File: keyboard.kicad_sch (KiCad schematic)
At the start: 52 parts, among them J1 TRRS, SW00 Key, SW01 Key, SW02 Key, SW03 Key, SW04 Key, SW05 Key, SW10 Key, SW11 Key, SW12 Key, SW13 Key, SW14 Key, SW15 Key, SW16 Key, SW17 Key, SW18 Key, SW20 Key, SW21 Key, SW22 Key, SW23 Key, SW24 Key, SW25 Key, SW26 Key, SW27 Key, SW28 Key, SW30 Key, SW31 Key, SW32 Key, SW33 Key, SW34 Key, SW35 Key, SW36 Key, SW37 Key, SW38 Key, SW40 Key, SW41 Key, SW42 Key, SW43 Key, SW44 Key, SW45 Key, SW46 Key, SW47 Key, SW48 Key, U1 ProMicro

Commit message: rename files
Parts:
- H1: footprint myles-keyboard:RightPlate -> keyboard:RightPlate; symbol myles-keyboard:RightPate -> keyboard:RightPate
- J1: footprint myles-keyboard:PJ-320A -> keyboard:PJ-320A; symbol myles-keyboard:PJ-320A -> keyboard:PJ-320A
- JP1, JP2: footprint myles-keyboard:Jumper -> keyboard:Jumper; symbol myles-keyboard:Jumper -> keyboard:Jumper
- JP3, JP4: footprint myles-keyboard:JumperSplit -> keyboard:JumperSplit; symbol myles-keyboard:JumperSplit -> keyboard:JumperSplit
- R1, R2: footprint myles-keyboard:SDR18 -> keyboard:SDR18
- SW00, SW04, SW05, SW10, SW14, SW20, SW30: footprint myles-keyboard:KeyLeft -> keyboard:KeyLeft; symbol myles-keyboard:Key -> keyboard:Key
- SW01, SW02, SW11, SW12, SW13, SW15, SW16, SW17, SW21, SW22, SW23, SW24, SW25, SW26, SW27, SW31, SW32, SW33, SW34, SW35, SW36, SW37, SW40, SW41, SW42, SW43, SW44, SW46, SW47: footprint myles-keyboard:Key -> keyboard:Key; symbol myles-keyboard:Key -> keyboard:Key
- SW03, SW18, SW28, SW38, SW45, SW48: footprint myles-keyboard:KeyRight -> keyboard:KeyRight; symbol myles-keyboard:Key -> keyboard:Key
- SW_RST1: footprint myles-keyboard:PTS636 -> keyboard:PTS636; symbol myles-keyboard:SW_Push -> keyboard:SW_Push
- U1: footprint myles-keyboard:ProMicro -> keyboard:ProMicro; symbol myles-keyboard:ProMicro -> keyboard:ProMicro

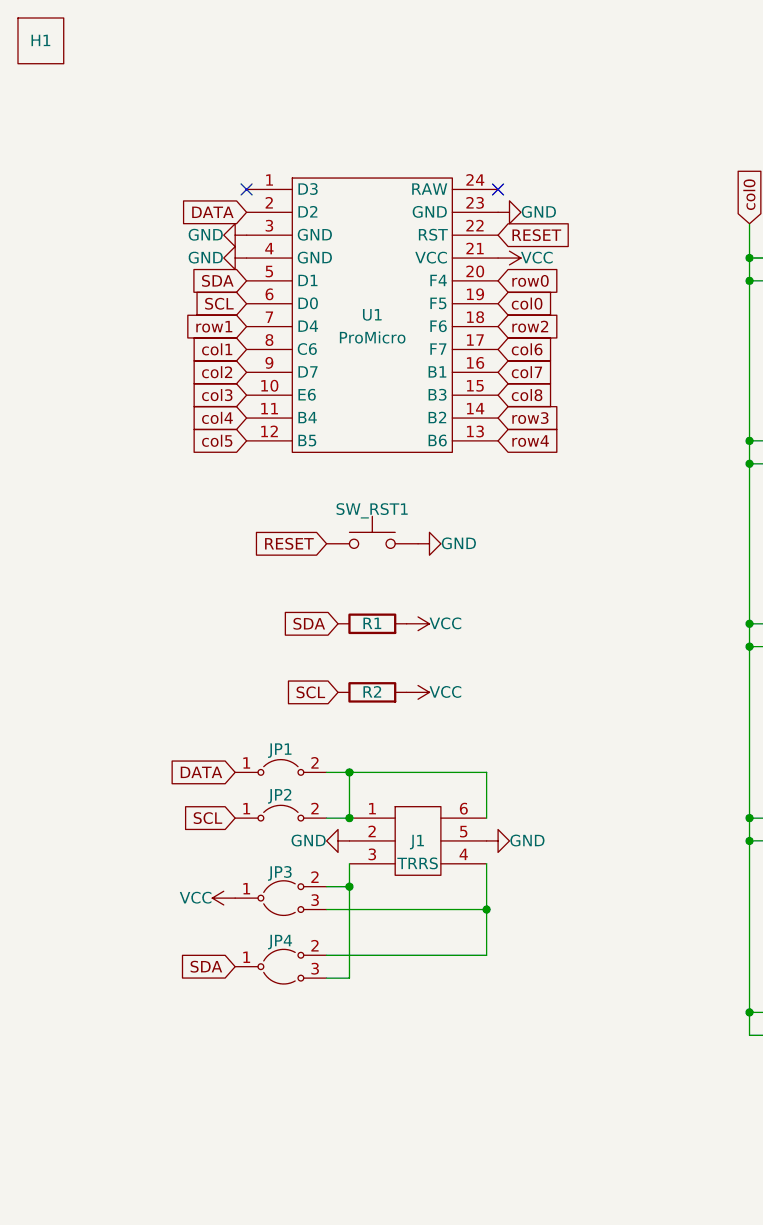
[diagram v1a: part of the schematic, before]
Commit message: add symbol and footprint for new thin reset button
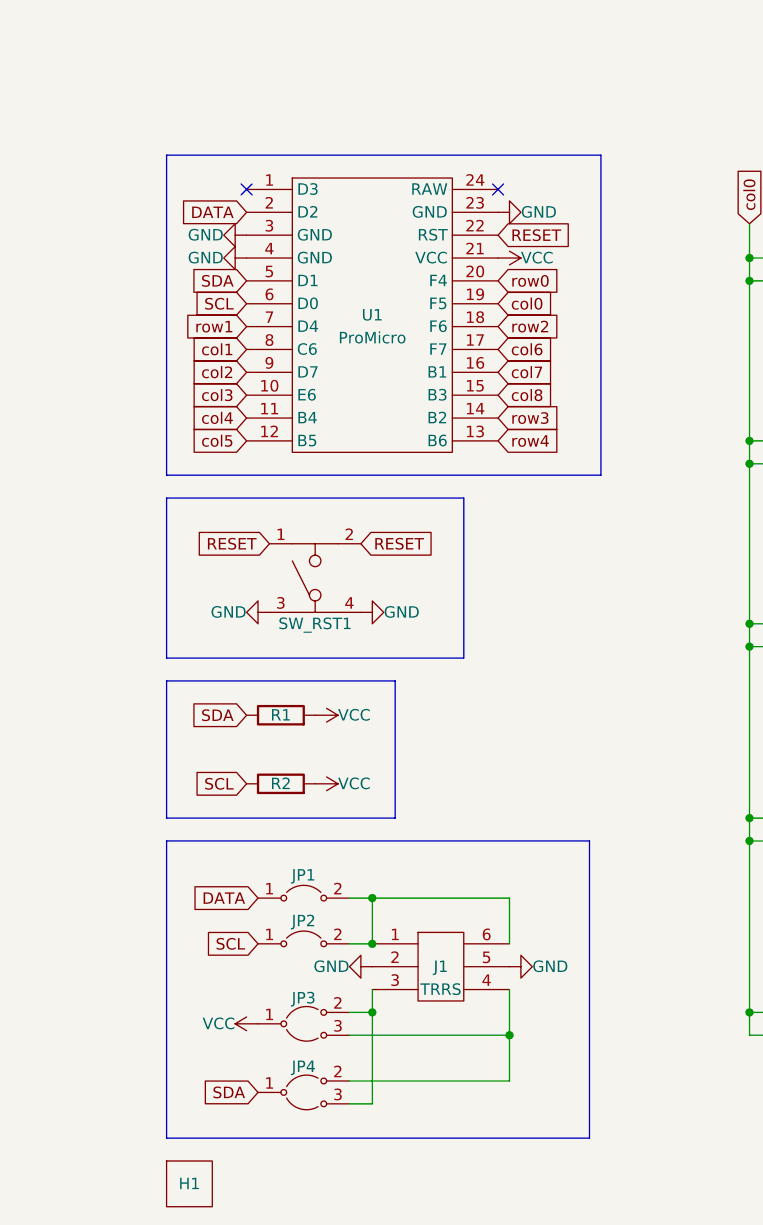
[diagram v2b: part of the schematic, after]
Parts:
- removed SW_RST1: SW_Push, keyboard:PTS636, symbol keyboard:SW_Push
- added SW_RST1: PTS525, keyboard:PTS525, symbol keyboard:PTS525
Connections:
- net GND: now also SW_RST1.3, SW_RST1.4
- net RESET: now also SW_RST1.1, SW_RST1.2
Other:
- moved on the sheet: H1, J1, JP1, JP2, JP3, JP4, R1, R2

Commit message: remove two thumb keys
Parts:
- removed SW04, SW05: Key, keyboard:KeyLeft, symbol keyboard:Key
- SW20, SW30: footprint keyboard:KeyLeft -> keyboard:Key
- SW40, SW41: footprint keyboard:Key -> keyboard:KeyLeft
- SW43: footprint keyboard:Key -> keyboard:KeyRight
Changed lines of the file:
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@@
   (junction (at 219.71 81.28) (diameter 0) (color 0 0 0 0)
   )
-  (junction (at 184.15 43.18) (diameter 0) (color 0 0 0 0)
-  )
   (junction (at 95.25 124.46) (diameter 0) (color 0 0 0 0)
   )
@@
   (junction (at 166.37 60.96) (diameter 0) (color 0 0 0 0)
   )
-  (junction (at 166.37 40.64) (diameter 0) (color 0 0 0 0)
-  )
   (junction (at 148.59 60.96) (diameter 0) (color 0 0 0 0)
   )
@@
   (junction (at 184.15 105.41) (diameter 0) (color 0 0 0 0)
   )
-  (junction (at 184.15 40.64) (diameter 0) (color 0 0 0 0)
-  )
   (junction (at 95.25 105.41) (diameter 0) (color 0 0 0 0)
   )
@@
   (junction (at 144.78 43.18) (diameter 0) (color 0 0 0 0)
   )
-  (junction (at 166.37 43.18) (diameter 0) (color 0 0 0 0)
-  )
   (junction (at 201.93 81.28) (diameter 0) (color 0 0 0 0)
   )
   (junction (at 198.12 83.82) (diameter 0) (color 0 0 0 0)
   )
-  (junction (at 198.12 43.18) (diameter 0) (color 0 0 0 0)
-  )
   (junction (at 95.25 40.64) (diameter 0) (color 0 0 0 0)
   )
   (junction (at 127 63.5) (diameter 0) (color 0 0 0 0)
   )
-  (junction (at 198.12 53.34) (diameter 0) (color 0 0 0 0)
-  )
   (junction (at 162.56 53.34) (diameter 0) (color 0 0 0 0)
   )
@@
   (junction (at 219.71 124.46) (diameter 0) (color 0 0 0 0)
   )
-  (junction (at 180.34 43.18) (diameter 0) (color 0 0 0 0)
-  )
   (junction (at 109.22 43.18) (diameter 0) (color 0 0 0 0)
   )
@@
   (junction (at 180.34 93.98) (diameter 0) (color 0 0 0 0)
   )
-  (junction (at 180.34 53.34) (diameter 0) (color 0 0 0 0)
-  )
   (junction (at 237.49 83.82) (diameter 0) (color 0 0 0 0)
   )
@@
   (no_connect (at 67.31 33.02))
   (no_connect (at 39.37 33.02))
-  (wire (pts (xy 162.56 53.34) (xy 180.34 53.34))
+  (wire (pts (xy 162.56 53.34) (xy 251.46 53.34))
     (stroke (width 0) (type default))
   )
@@
     (stroke (width 0) (type default))
   )
-  (wire (pts (xy 180.34 40.64) (xy 180.34 43.18))
-    (stroke (width 0) (type default))
-  )
   (wire (pts (xy 232.41 102.87) (xy 233.68 102.87))
     (stroke (width 0) (type default))
@@
     (stroke (width 0) (type default))
   )
-  (wire (pts (xy 166.37 36.83) (xy 166.37 40.64))
+  (wire (pts (xy 166.37 36.83) (xy 166.37 60.96))
     (stroke (width 0) (type default))
   )
@@
     (stroke (width 0) (type default))
   )
-  (wire (pts (xy 198.12 53.34) (xy 251.46 53.34))
-    (stroke (width 0) (type default))
-  )
   (wire (pts (xy 127 72.39) (xy 127 73.66))
     (stroke (width 0) (type default))
@@
     (stroke (width 0) (type default))
   )
-  (wire (pts (xy 184.15 40.64) (xy 184.15 43.18))
-    (stroke (width 0) (type default))
-  )
   (wire (pts (xy 251.46 93.98) (xy 233.68 93.98))
     (stroke (width 0) (type default))
@@
     (stroke (width 0) (type default))
   )
-  (wire (pts (xy 166.37 40.64) (xy 168.91 40.64))
-    (stroke (width 0) (type default))
-  )
   (wire (pts (xy 180.34 124.46) (xy 180.34 127))
     (stroke (width 0) (type default))
@@
     (stroke (width 0) (type default))
   )
-  (wire (pts (xy 196.85 43.18) (xy 198.12 43.18))
-    (stroke (width 0) (type default))
-  )
   (wire (pts (xy 130.81 105.41) (xy 130.81 124.46))
     (stroke (width 0) (type default))
@@
     (stroke (width 0) (type default))
   )
-  (wire (pts (xy 184.15 40.64) (xy 186.69 40.64))
-    (stroke (width 0) (type default))
-  )
   (wire (pts (xy 215.9 127) (xy 215.9 128.27))
     (stroke (width 0) (type default))
@@
     (stroke (width 0) (type default))
   )
-  (wire (pts (xy 179.07 40.64) (xy 180.34 40.64))
-    (stroke (width 0) (type default))
-  )
   (wire (pts (xy 50.8 134.62) (xy 53.34 134.62))
     (stroke (width 0) (type default))
@@
     (stroke (width 0) (type default))
   )
-  (wire (pts (xy 166.37 43.18) (xy 166.37 60.96))
-    (stroke (width 0) (type default))
-  )
   (wire (pts (xy 127 81.28) (xy 127 83.82))
     (stroke (width 0) (type default))
@@
     (stroke (width 0) (type default))
   )
-  (wire (pts (xy 180.34 43.18) (xy 179.07 43.18))
-    (stroke (width 0) (type default))
-  )
   (wire (pts (xy 201.93 124.46) (xy 204.47 124.46))
     (stroke (width 0) (type default))
@@
     (stroke (width 0) (type default))
   )
-  (wire (pts (xy 198.12 43.18) (xy 198.12 40.64))
-    (stroke (width 0) (type default))
-  )
   (wire (pts (xy 232.41 105.41) (xy 233.68 105.41))
     (stroke (width 0) (type default))
@@
     (stroke (width 0) (type default))
   )
-  (wire (pts (xy 180.34 44.45) (xy 180.34 43.18))
-    (stroke (width 0) (type default))
-  )
   (wire (pts (xy 127 60.96) (xy 127 63.5))
     (stroke (width 0) (type default))
@@
     (stroke (width 0) (type default))
   )
-  (wire (pts (xy 198.12 52.07) (xy 198.12 53.34))
-    (stroke (width 0) (type default))
-  )
   (wire (pts (xy 161.29 124.46) (xy 162.56 124.46))
     (stroke (width 0) (type default))
@@
     (stroke (width 0) (type default))
   )
-  (wire (pts (xy 180.34 52.07) (xy 180.34 53.34))
-    (stroke (width 0) (type default))
-  )
   (wire (pts (xy 214.63 60.96) (xy 215.9 60.96))
     (stroke (width 0) (type default))
@@
     (stroke (width 0) (type default))
   )
-  (wire (pts (xy 198.12 40.64) (xy 196.85 40.64))
-    (stroke (width 0) (type default))
-  )
   (wire (pts (xy 95.25 81.28) (xy 97.79 81.28))
     (stroke (width 0) (type default))
   )
-  (wire (pts (xy 184.15 36.83) (xy 184.15 40.64))
-    (stroke (width 0) (type default))
-  )
   (wire (pts (xy 53.34 111.76) (xy 50.8 111.76))
     (stroke (width 0) (type default))
@@
     (stroke (width 0) (type default))
   )
-  (wire (pts (xy 198.12 44.45) (xy 198.12 43.18))
-    (stroke (width 0) (type default))
-  )
   (wire (pts (xy 125.73 40.64) (xy 127 40.64))
     (stroke (width 0) (type default))
@@
     (stroke (width 0) (type default))
   )
-  (wire (pts (xy 184.15 43.18) (xy 184.15 60.96))
+  (wire (pts (xy 184.15 36.83) (xy 184.15 60.96))
     (stroke (width 0) (type default))
   )
@@
     (stroke (width 0) (type default))
   )
-  (wire (pts (xy 184.15 43.18) (xy 186.69 43.18))
-    (stroke (width 0) (type default))
-  )
   (wire (pts (xy 107.95 105.41) (xy 109.22 105.41))
     (stroke (width 0) (type default))
@@
     (stroke (width 0) (type default))
   )
-  (wire (pts (xy 180.34 53.34) (xy 198.12 53.34))
-    (stroke (width 0) (type default))
-  )
   (wire (pts (xy 107.95 127) (xy 109.22 127))
     (stroke (width 0) (type default))
@@
     (stroke (width 0) (type default))
   )
-  (wire (pts (xy 166.37 40.64) (xy 166.37 43.18))
-    (stroke (width 0) (type default))
-  )
   (wire (pts (xy 95.25 124.46) (xy 95.25 127))
     (stroke (width 0) (type default))
@@
     (stroke (width 0) (type default))
   )
-  (wire (pts (xy 166.37 43.18) (xy 168.91 43.18))
-    (stroke (width 0) (type default))
-  )
   (wire (pts (xy 162.56 63.5) (xy 162.56 64.77))
     (stroke (width 0) (type default))
@@
     )
   )
-  (symbol (lib_id "keyboard:Key") (at 173.99 41.91 0) (unit 1)
-    (in_bom yes) (on_board yes) (dnp no)
-    (property "Reference" "SW04" (at 173.99 36.195 0) (do_not_autoplace)
-      (effects (font (size 1.27 1.27)))
-    )
-    (property "Value" "Key" (at 173.99 47.625 0) (do_not_autoplace)
-      (effects (font (size 1.27 1.27)) hide)
-    )
-    (property "Footprint" "keyboard:KeyLeft" (at 173.99 41.91 0)
-      (effects (font (size 1.27 1.27)) hide)
-    )
-    (property "Datasheet" "" (at 173.99 41.91 0)
-      (effects (font (size 1.27 1.27)) hide)
-    )
-    (pin "1")
-    (pin "2")
-    (pin "3")
-    (pin "4")
-    (pin "5")
-    (pin "6")
-    (instances
-      (project "keyboard"
-        (path "/55a8c568-8b67-4781-bca4-b9ba3160a3cd"
-          (reference "SW04") (unit 1)
-        )
-      )
-    )
-  )
   (symbol (lib_id "keyboard:Key") (at 227.33 62.23 0) (unit 1)
     (in_bom yes) (on_board yes) (dnp no) (fields_autoplaced)
@@
       (effects (font (size 1.27 1.27)) hide)
     )
-    (property "Footprint" "keyboard:KeyLeft" (at 102.87 82.55 0)
+    (property "Footprint" "keyboard:Key" (at 102.87 82.55 0)
       (effects (font (size 1.27 1.27)) hide)
     )
@@
       (effects (font (size 1.27 1.27)) hide)
     )
-    (property "Footprint" "keyboard:Key" (at 156.21 125.73 0)
+    (property "Footprint" "keyboard:KeyRight" (at 156.21 125.73 0)
       (effects (font (size 1.27 1.27)) hide)
     )
@@
       (effects (font (size 1.27 1.27)) hide)
     )
-    (property "Footprint" "keyboard:KeyLeft" (at 102.87 104.14 0)
+    (property "Footprint" "keyboard:Key" (at 102.87 104.14 0)
       (effects (font (size 1.27 1.27)) hide)
     )
@@
       (effects (font (size 1.27 1.27)) hide)
     )
-    (property "Footprint" "keyboard:Key" (at 120.65 125.73 0)
+    (property "Footprint" "keyboard:KeyLeft" (at 120.65 125.73 0)
       (effects (font (size 1.27 1.27)) hide)
     )
@@
     )
   )
-  (symbol (lib_id "keyboard:Key") (at 191.77 41.91 0) (unit 1)
-    (in_bom yes) (on_board yes) (dnp no)
-    (property "Reference" "SW05" (at 191.77 36.195 0) (do_not_autoplace)
-      (effects (font (size 1.27 1.27)))
-    )
-    (property "Value" "Key" (at 191.77 47.625 0) (do_not_autoplace)
-      (effects (font (size 1.27 1.27)) hide)
-    )
-    (property "Footprint" "keyboard:KeyLeft" (at 191.77 41.91 0)
-      (effects (font (size 1.27 1.27)) hide)
-    )
-    (property "Datasheet" "" (at 191.77 41.91 0)
-      (effects (font (size 1.27 1.27)) hide)
-    )
-    (pin "1")
-    (pin "2")
-    (pin "3")
-    (pin "4")
-    (pin "5")
-    (pin "6")
-    (instances
-      (project "keyboard"
-        (path "/55a8c568-8b67-4781-bca4-b9ba3160a3cd"
-          (reference "SW05") (unit 1)
-        )
-      )
-    )
-  )
   (symbol (lib_id "keyboard:Key") (at 138.43 125.73 0) (unit 1)
     (in_bom yes) (on_board yes) (dnp no) (fields_autoplaced)
@@
       (effects (font (size 1.27 1.27)) hide)
     )
-    (property "Footprint" "keyboard:Key" (at 102.87 125.73 0)
+    (property "Footprint" "keyboard:KeyLeft" (at 102.87 125.73 0)
       (effects (font (size 1.27 1.27)) hide)
     )

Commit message: fix more traces
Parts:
- SW15, SW25, SW35: footprint keyboard:Key -> keyboard:KeyRight
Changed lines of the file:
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@@
       (effects (font (size 1.27 1.27)) hide)
     )
-    (property "Footprint" "keyboard:Key" (at 191.77 82.55 0)
+    (property "Footprint" "keyboard:KeyRight" (at 191.77 82.55 0)
       (effects (font (size 1.27 1.27)) hide)
     )
@@
       (effects (font (size 1.27 1.27)) hide)
     )
-    (property "Footprint" "keyboard:Key" (at 191.77 62.23 0)
+    (property "Footprint" "keyboard:KeyRight" (at 191.77 62.23 0)
       (effects (font (size 1.27 1.27)) hide)
     )
@@
       (effects (font (size 1.27 1.27)) hide)
     )
-    (property "Footprint" "keyboard:Key" (at 191.77 104.14 0)
-      (effects (font (size 1.27 1.27)) hide)
-    )
+    (property "Footprint" "keyboard:KeyRight" (at 191.77 104.14 0)
+      (effects (font (size 1.27 1.27)) hide)
+    )

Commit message: update reset button
- move 3d model into directory
- update PTS525 to PTS526
- centre align reset button with pro micro
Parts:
- SW_RST1: value PTS525 -> PTS526; symbol keyboard:PTS525 -> keyboard:PTS526
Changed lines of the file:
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@@
     )
   )
-  (symbol (lib_id "keyboard:PTS525") (at 46.99 76.2 0) (unit 1)
+  (symbol (lib_id "keyboard:PTS526") (at 46.99 76.2 0) (unit 1)
     (in_bom yes) (on_board yes) (dnp no)
-    (property "Reference" "SW_RST1" (at 46.99 81.28 0) (do_not_autoplace)
+    (property "Reference" "SW_RST1" (at 46.99 81.28 0)
       (effects (font (size 1.27 1.27)))
     )
-    (property "Value" "PTS525" (at 46.99 83.82 0)
+    (property "Value" "PTS526" (at 46.99 83.82 0)
       (effects (font (size 1.27 1.27)) hide)
     )
